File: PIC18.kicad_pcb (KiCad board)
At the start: 2 copper layers, 17 parts, among them J1 Conn_02x20_Counter_Clockwise, J2 Conn_01x06_Pin, J3 USB_A, U1 PIC18F4321-I/P, U2 LM4040DBZ-4.1, U3 FT230XS, Y1 8 MHz

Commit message: footprint and step assignment
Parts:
- J1: footprint PinSockets:PinSocket_2x20_Counter_Clockwise_P1.27mm_Vertical -> PinSockets:PinSocket_2x20_Counter_Clockwise_P2.54mm_Vertical
- J2: footprint Connector_PinHeader_1.27mm:PinHeader_1x06_P1.27mm_Vertical -> Connector_PinHeader_2.54mm:PinHeader_1x06_P2.54mm_Vertical
- moved J1 12.5 mm to (207.8, 72.4)

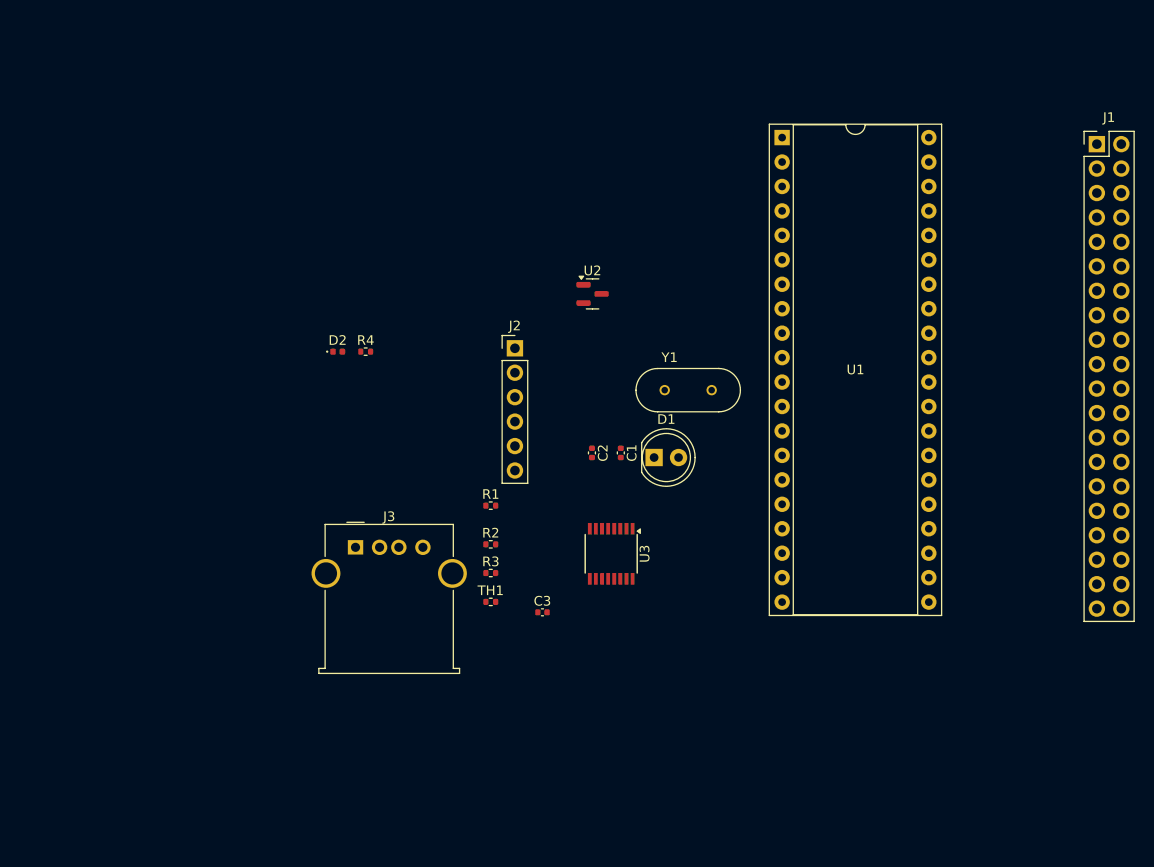
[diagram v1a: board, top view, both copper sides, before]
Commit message: yet more footprint assignment
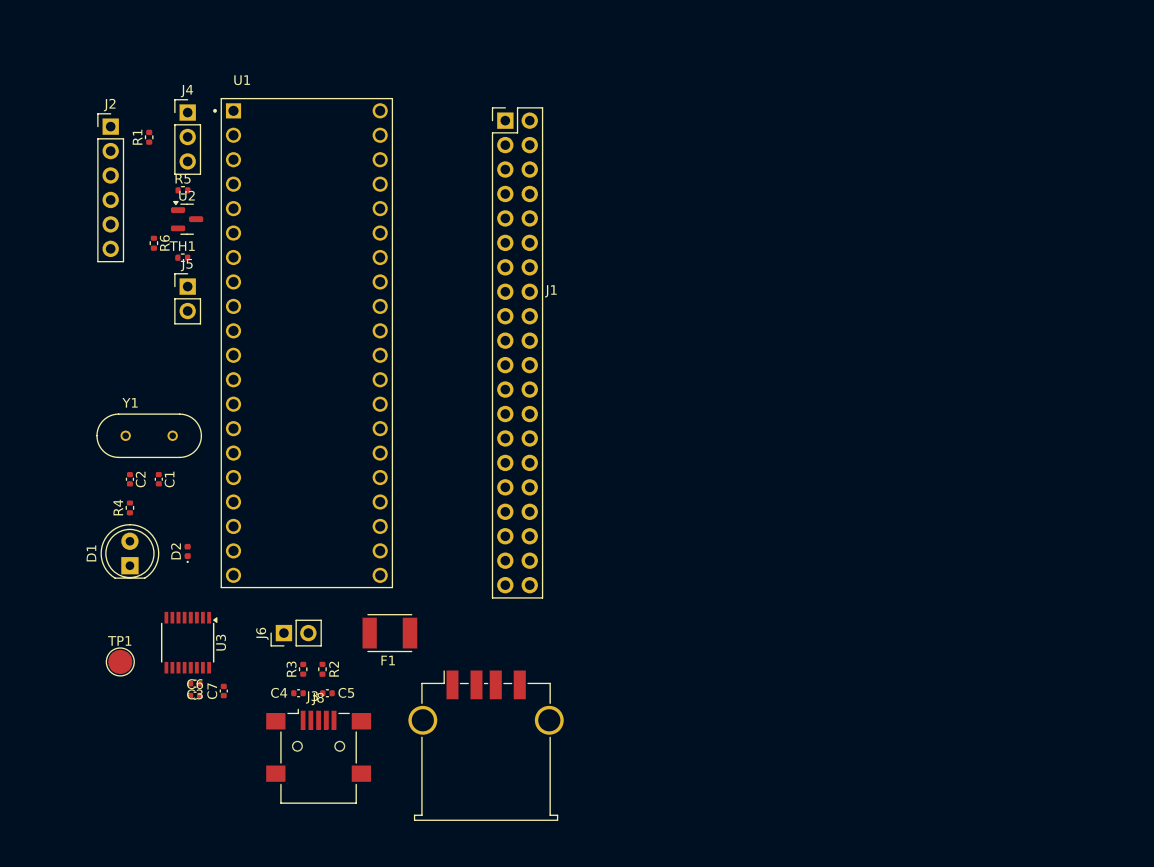
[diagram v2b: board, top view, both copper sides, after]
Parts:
- added C4: 47pf, Capacitor_SMD:C_0402_1005Metric, F.Cu at (121.5, 129.5)
- added C5: 47pf, Capacitor_SMD:C_0402_1005Metric, F.Cu at (124.5, 129.5)
- added C6: 100n, Capacitor_SMD:C_0402_1005Metric, F.Cu at (110.8, 129.7)
- added C7: 4.7u, Capacitor_SMD:C_0402_1005Metric, F.Cu at (113.8, 129.3)
- added F1: MF-MSMF200-2, MF-MSMF200-2:FUSER_MF-MSMF200-2, F.Cu at (131.0, 123.2)
- added J4: Conn_01x03, Connector_PinHeader_2.54mm:PinHeader_1x03_P2.54mm_Vertical, F.Cu at (110.0, 69.2)
- added J5: Conn_01x02, Connector_PinHeader_2.54mm:PinHeader_1x02_P2.54mm_Vertical, F.Cu at (110.0, 87.2)
- added J6: Conn_01x02, Connector_PinHeader_2.54mm:PinHeader_1x02_P2.54mm_Vertical, F.Cu at (120.0, 123.2)
- added J8: USB_OTG, Connector_USB:USB_Mini-B_Lumberg_2486_01_Horizontal, F.Cu at (123.6, 135.0)
- added R5: 33, Resistor_SMD:R_0402_1005Metric, F.Cu at (109.5, 77.2)
- added R6: 220, Resistor_SMD:R_0402_1005Metric, F.Cu at (106.5, 82.7)
- added TP1: TestPoint, TestPoint:TestPoint_Pad_D2.5mm, F.Cu at (103.0, 126.2)
- J2: value Conn_01x06_Pin -> Conn_01x06
- J3: footprint Connector_USB:USB_A_Molex_67643_Horizontal -> Connector_USB:USB_A_TE_292303-7_Horizontal
- U1: value PIC18F4321-I/P -> PIC18F4620; footprint Package_DIP:DIP-40_W15.24mm_Socket -> DILB40P-223TLF:AMPHENOL_DILB40P-223TLF
- moved J1 62.3 mm to (145.5, 70.0)
- moved Y1 56.2 mm to (106.0, 102.7)
- moved D1 55.6 mm to (104.0, 116.2), turned to 90 degrees
- moved U1 53.8 mm to (122.4, 93.1)
- moved R1 52.2 mm to (106.0, 71.7), turned to 90 degrees
- moved C1 48.1 mm to (107.0, 107.3)
- moved C2 48.1 mm to (104.0, 107.3)
- moved TH1 48.0 mm to (109.5, 84.2)
- moved J2 47.9 mm to (102.0, 70.6)
- moved U3 45.0 mm to (110.0, 124.2)
- moved U2 42.8 mm to (109.9, 80.2)
- moved C3 36.8 mm to (110.8, 128.5), turned to 180 degrees
- moved R4 29.4 mm to (104.0, 110.2), turned to 90 degrees
- moved D2 26.0 mm to (110.0, 114.8), turned to 90 degrees
- moved J3 24.7 mm to (141.0, 135.0)
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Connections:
- J3 pad 1: unconnected-(J3-VBUS-Pad1) -> Net-(J3-VBUS)
- TH1 pad 1: unconnected-(TH1-Pad1) -> /VTHERM
- TH1 pad 2: unconnected-(TH1-Pad2) -> GND
- U2 pad 1: unconnected-(U2-K-Pad1) -> /RA3/AN3/VREF+
- U2 pad 2: unconnected-(U2-A-Pad2) -> GND
- U3 pad 1: /RC6/TX/CK -> /RC7/RX/DT
- U3 pad 4: /RC7/RX/DT -> /RC6/TX/CK

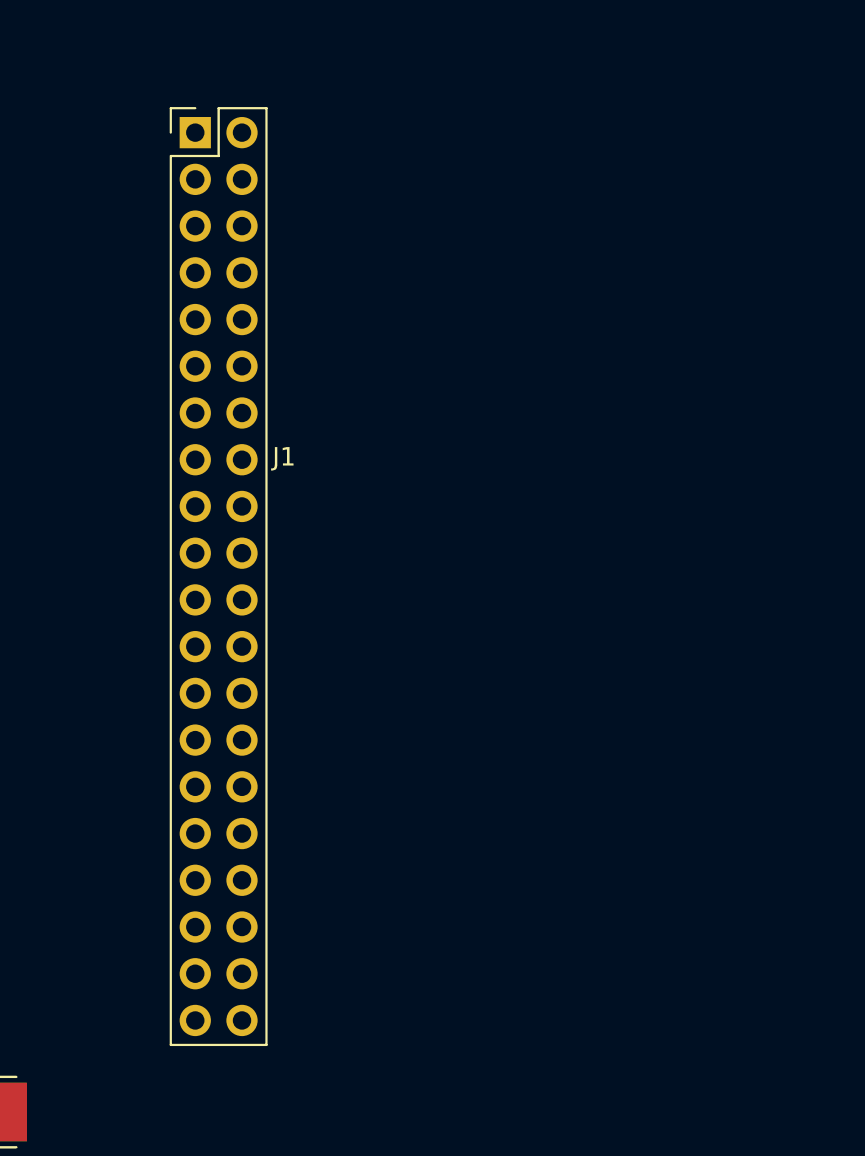
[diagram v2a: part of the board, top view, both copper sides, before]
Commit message: added Zener and colored pin headers
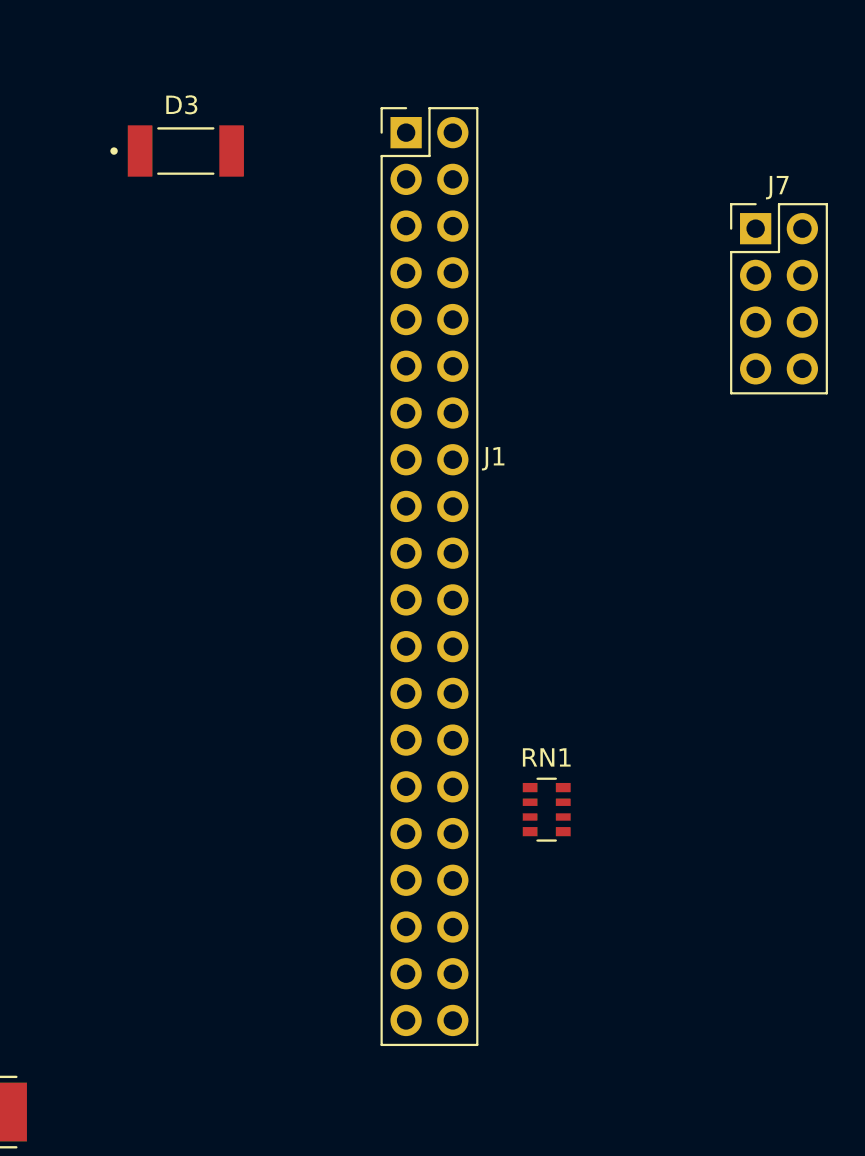
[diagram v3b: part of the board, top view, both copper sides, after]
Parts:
- added D3: D_Zener, ZM4748A_L0G:DIOMELF5124N, F.Cu at (142.5, 71.0)
- added J7: Conn_01x08, Connector_PinHeader_2.54mm:PinHeader_2x04_P2.54mm_Vertical, F.Cu at (173.5, 75.2)
- added RN1: R_Pack04, Resistor_SMD:R_Array_Convex_4x0603, F.Cu at (162.1, 106.8)
- moved J1 11.5 mm to (157.0, 70.0)

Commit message: Updates
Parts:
- added D4: D_Zener, ZM4748A_L0G:DIOMELF5124N, F.Cu at (138.5, 77.7)
- added D5: D_Zener, ZM4748A_L0G:DIOMELF5124N, F.Cu at (138.5, 73.3)
- added D6: D_Zener, ZM4748A_L0G:DIOMELF5124N, F.Cu at (138.5, 69.0)
- added D7: D_Zener, ZM4748A_L0G:DIOMELF5124N, F.Cu at (162.0, 71.0)
- added D8: ZMM5V1, ZM4748A_L0G:DIOMELF5124N, F.Cu at (166.3, 71.0)
- added H1: MountingHole_Pad, MountingHole:MountingHole_4.3mm_M4_ISO14580_Pad_TopBottom, F.Cu at (97.0, 65.0)
- added H2: MountingHole_Pad, MountingHole:MountingHole_4.3mm_M4_ISO14580_Pad_TopBottom, F.Cu at (186.0, 65.0)
- added H3: MountingHole_Pad, MountingHole:MountingHole_4.3mm_M4_ISO14580_Pad_TopBottom, F.Cu at (96.0, 139.0)
- added H4: MountingHole_Pad, MountingHole:MountingHole_4.3mm_M4_ISO14580_Pad_TopBottom, F.Cu at (188.0, 142.0)
- added J10: Port B, PinHeaders:PinHeader_2x04_P2.54mm_Vertical_Yellow, F.Cu at (177.5, 124.4)
- added J11: Port C, PinHeaders:PinHeader_2x04_P2.54mm_Vertical_Blue, F.Cu at (177.5, 96.9)
- added J12: Port D, PinHeaders:PinHeader_2x04_P2.54mm_Vertical_White, F.Cu at (177.5, 110.9)
- added J13: Conn_01x03, Connector_PinHeader_2.54mm:PinHeader_1x03_P2.54mm_Vertical, F.Cu at (141.0, 102.0)
- added J14: Conn_01x03, Connector_PinHeader_2.54mm:PinHeader_1x03_P2.54mm_Vertical, F.Cu at (158.0, 133.5)
- added J9: Port E, PinHeaders:PinHeader_2x04_P2.54mm_Vertical_Green, F.Cu at (177.5, 83.0)
- added R10: 220, Resistor_SMD:R_0402_1005Metric, F.Cu at (173.0, 75.0)
- added R11: 220, Resistor_SMD:R_0402_1005Metric, F.Cu at (147.0, 69.5)
- added R12: 220, Resistor_SMD:R_0402_1005Metric, F.Cu at (147.0, 71.5)
- added R13: 220, Resistor_SMD:R_0402_1005Metric, F.Cu at (147.0, 73.5)
- added R14: 220, Resistor_SMD:R_0402_1005Metric, F.Cu at (147.0, 75.5)
- added R15: 100, Resistor_SMD:R_0402_1005Metric, F.Cu at (173.0, 87.2)
- added R16: 1k, Resistor_SMD:R_0402_1005Metric, F.Cu at (173.0, 88.2)
- added R17: 10k, Resistor_SMD:R_0402_1005Metric, F.Cu at (173.0, 89.2)
- added R18: 100k, Resistor_SMD:R_0402_1005Metric, F.Cu at (173.0, 90.3)
- added R19: 220, Resistor_SMD:R_0402_1005Metric, F.Cu at (153.8, 133.1)
- added R20: 220, Resistor_SMD:R_0402_1005Metric, F.Cu at (153.8, 136.1)
- added R21: 220, Resistor_SMD:R_0402_1005Metric, F.Cu at (153.8, 139.1)
- added R7: 220, Resistor_SMD:R_0402_1005Metric, F.Cu at (173.0, 69.0)
- added R8: 220, Resistor_SMD:R_0402_1005Metric, F.Cu at (173.0, 71.0)
- added R9: 220, Resistor_SMD:R_0402_1005Metric, F.Cu at (173.0, 73.0)
- added RN2: 220, Resistor_SMD:R_Array_Convex_4x0603, F.Cu at (173.0, 124.8)
- added RN3: 220, Resistor_SMD:R_Array_Convex_4x0603, F.Cu at (173.0, 131.5)
- added RN4: 220, Resistor_SMD:R_Array_Convex_4x0603, F.Cu at (173.0, 97.8)
- added RN5: 220, Resistor_SMD:R_Array_Convex_4x0603, F.Cu at (173.1, 103.8)
- added RN6: 220, Resistor_SMD:R_Array_Convex_4x0603, F.Cu at (173.1, 111.8)
- added RN7: 220, Resistor_SMD:R_Array_Convex_4x0603, F.Cu at (173.1, 117.8)
- J7: value Conn_01x08 -> USB_OTG; footprint Connector_PinHeader_2.54mm:PinHeader_2x04_P2.54mm_Vertical -> Connector_USB:USB_Mini-B_Lumberg_2486_01_Horizontal
- J8: value USB_OTG -> Port A; footprint Connector_USB:USB_Mini-B_Lumberg_2486_01_Horizontal -> PinHeaders:PinHeader_2x04_P2.54mm_Vertical_Red
- RN1: value R_Pack04 -> 220
- moved J8 84.9 mm to (177.5, 69.4)
- moved J7 79.6 mm to (122.5, 136.4)
- moved RN1 25.2 mm to (173.0, 84.0)
- moved D3 11.7 mm to (138.5, 82.0), turned to 180 degrees
- moved R6 8.66 mm to (112.5, 76.5)
- moved J1 2.68 mm to (154.5, 68.9)
- moved U2 1.64 mm to (110.4, 81.8)
- moved J5 0.55 mm to (110.5, 87.5)
- moved R5 0.51 mm to (109.5, 77.8)
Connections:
- J1 pad 7: unconnected-(J1-Pin_7-Pad7) -> /RA5/AN4/SS*/HLVDIN/C2OUT
- J7 pad 1: unconnected-(J7-Pin_1-Pad1) -> VCC
- J7 pad 2: unconnected-(J7-Pin_2-Pad2) -> Net-(J3-D-)
- J7 pad 3: unconnected-(J7-Pin_3-Pad3) -> Net-(J3-D+)
- J7 pad 5: unconnected-(J7-Pin_5-Pad5) -> GND
- J7 pad 6: unconnected-(J7-Pin_6-Pad6) -> GND
- J8 pad 1: VCC -> Net-(J8-Pin_1)
- J8 pad 2: Net-(J3-D-) -> Net-(J8-Pin_2)
- J8 pad 3: Net-(J3-D+) -> Net-(J8-Pin_3)
- J8 pad 4: unconnected-(J8-ID-Pad4) -> Net-(J8-Pin_4)
- J8 pad 5: GND -> Net-(J8-Pin_5)
- J8 pad 6: GND -> Net-(J8-Pin_6)
- RN1 pad 2: unconnected-(RN1-R2.1-Pad2) -> Net-(J9-Pin_3)
- RN1 pad 3: unconnected-(RN1-R3.1-Pad3) -> Net-(J9-Pin_2)
- RN1 pad 4: unconnected-(RN1-R4.1-Pad4) -> Net-(J9-Pin_1)
- RN1 pad 5: unconnected-(RN1-R4.2-Pad5) -> /RE0/RD*/AN5
- RN1 pad 6: unconnected-(RN1-R3.2-Pad6) -> /RE1/WR*/AN6
- RN1 pad 7: unconnected-(RN1-R2.2-Pad7) -> /RE2/CS*/AN7

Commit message: Updates
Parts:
- J1: value Conn_02x20_Counter_Clockwise -> Conn_02x20_Odd_Even; footprint PinSockets:PinSocket_2x20_Counter_Clockwise_P2.54mm_Vertical -> Connector_PinHeader_2.54mm:PinHeader_2x20_P2.54mm_Vertical
- moved J1 2.04 mm to (152.5, 69.0)
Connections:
- J1 pad 10: /RE2/CS*/AN7 -> /RB3/AN9/CCP2(1)
- J1 pad 11: VCC -> /RA4/T0CKI/C1OUT
- J1 pad 12: GND -> /RB2/INT2/AN8
- J1 pad 13: /OSC1/CLKI/RA7 -> /RA5/AN4/SS*/HLVDIN/C2OUT
- J1 pad 14: /OSC2/CLKO/RA6 -> /RB1/INT1/AN10
- J1 pad 15: /RC0/T1OSO/T13CKI -> /RE0/RD*/AN5
- J1 pad 16: /RC1/T1OSI/CCP2(1) -> /RB0/INT0/FLT0/AN12
- J1 pad 17: /RC2/CCP1/P1A -> /RE1/WR*/AN6
- J1 pad 18: /RC3/SCK/SCL -> VCC
- J1 pad 19: /RD0/PSP0 -> /RE2/CS*/AN7
- J1 pad 2: /RA0/AN0 -> /RB7/KBI3/PGD
- J1 pad 20: /RD1/PSP1 -> GND
- J1 pad 21: /RD2/PSP2 -> VCC
- J1 pad 22: /RD3/PSP3 -> /RD7/PSP7/P1D
- J1 pad 23: /RC4/SDI/SDA -> GND
- J1 pad 24: /RC5/SDO -> /RD6/PSP6/P1C
- J1 pad 25: /RC6/TX/CK -> /OSC1/CLKI/RA7
- J1 pad 26: /RC7/RX/DT -> /RD5/PSP5/P1B
- J1 pad 27: /RD4/PSP4 -> /OSC2/CLKO/RA6
- J1 pad 28: /RD5/PSP5/P1B -> /RD4/PSP4
- J1 pad 29: /RD6/PSP6/P1C -> /RC0/T1OSO/T13CKI
- J1 pad 3: /RA1/AN1 -> /RA0/AN0
- J1 pad 30: /RD7/PSP7/P1D -> /RC7/RX/DT
- J1 pad 31: GND -> /RC1/T1OSI/CCP2(1)
- J1 pad 32: VCC -> /RC6/TX/CK
- J1 pad 33: /RB0/INT0/FLT0/AN12 -> /RC2/CCP1/P1A
- J1 pad 34: /RB1/INT1/AN10 -> /RC5/SDO
- J1 pad 35: /RB2/INT2/AN8 -> /RC3/SCK/SCL
- J1 pad 36: /RB3/AN9/CCP2(1) -> /RC4/SDI/SDA
- J1 pad 37: /RB4/KBI0/AN11 -> /RD0/PSP0
- J1 pad 38: /RB5/KBI1/PGM -> /RD3/PSP3
- J1 pad 39: /RB6/KBI2/PGC -> /RD1/PSP1
- J1 pad 4: /RA2/AN2/VREF-/CVREF -> /RB6/KBI2/PGC
- J1 pad 40: /RB7/KBI3/PGD -> /RD2/PSP2
- J1 pad 5: /RA3/AN3/VREF+ -> /RA1/AN1
- J1 pad 6: /RA4/T0CKI/C1OUT -> /RB5/KBI1/PGM
- J1 pad 7: /RA5/AN4/SS*/HLVDIN/C2OUT -> /RA2/AN2/VREF-/CVREF
- J1 pad 8: /RE0/RD*/AN5 -> /RB4/KBI0/AN11
- J1 pad 9: /RE1/WR*/AN6 -> /RA3/AN3/VREF+
